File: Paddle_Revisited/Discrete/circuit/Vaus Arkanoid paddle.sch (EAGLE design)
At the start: 22 parts, among them IC1 4040N, IC2 74165N, IC3 74LS00N, IC4 LM556N

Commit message: Cleanup and organization of some directories
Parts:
- added C9: 100nf, rcl:C-EU050-024X044
- C2: value 15n -> 10n
- R3: value 1k -> 1k5
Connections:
- net DOUT: now also C9.1
- net GND: now also C9.2
- net N$15: now also R5.A; no longer R5.E
- net N$22: now also R5.E; no longer R5.A
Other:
- note added: "VAUS ARKANOID PADDLE FOR MSX"
- note removed: "TAITO ARKANOID PADDLE FOR MSX"
- moved on the sheet: K1

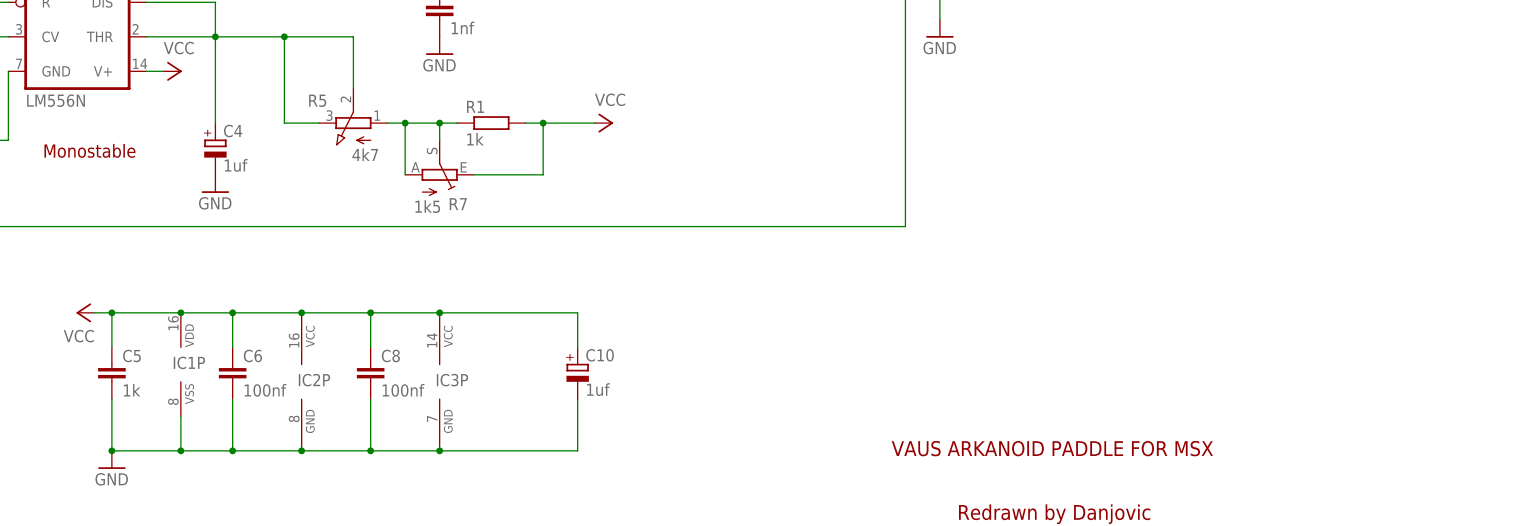
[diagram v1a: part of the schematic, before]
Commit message: Updated component values
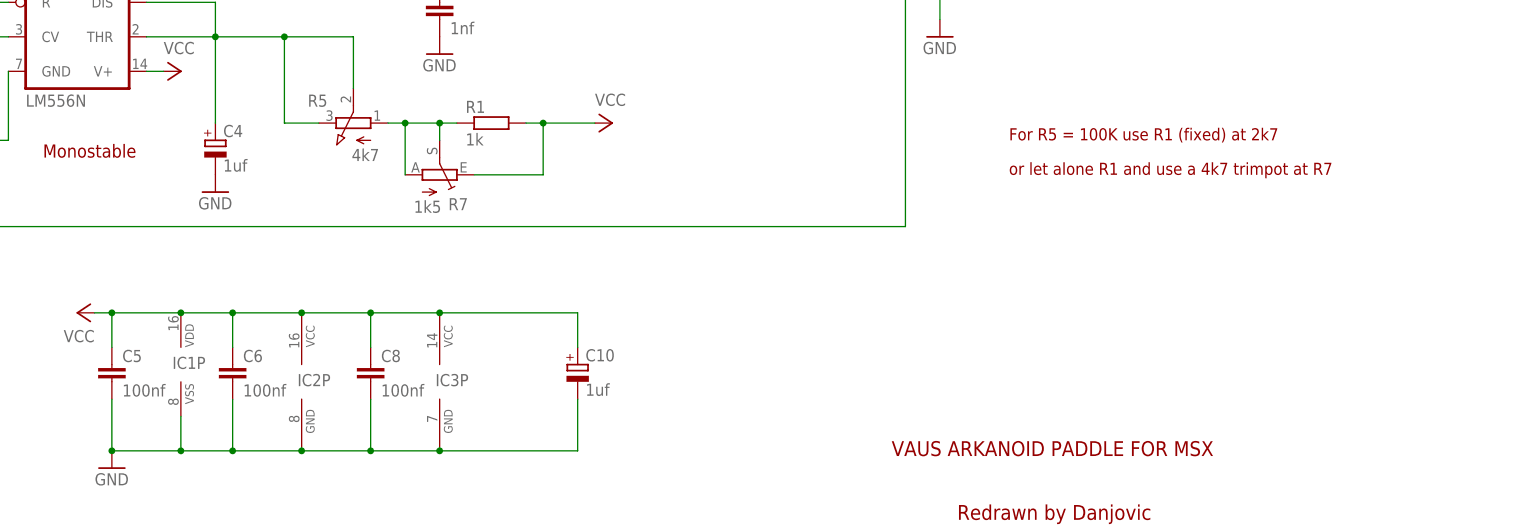
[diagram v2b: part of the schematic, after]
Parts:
- C5: value 1k -> 100nf
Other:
- note added: "For R5 = 100K use R1 (fixed) at 2k7"
- note added: "or let alone R1 and use a 4k7 trimpot at R7"
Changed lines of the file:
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@@
 <part name="P+8" library="supply1" deviceset="VCC" device=""/>
 <part name="C4" library="rcl" deviceset="CPOL-EU" device="E2-4" value="1uf"/>
-<part name="C5" library="rcl" deviceset="C-EU" device="050-024X044" value="1k"/>
+<part name="C5" library="rcl" deviceset="C-EU" device="050-024X044" value="100nf"/>
 <part name="C6" library="rcl" deviceset="C-EU" device="050-024X044" value="100nf"/>
 <part name="C8" library="rcl" deviceset="C-EU" device="050-024X044" value="100nf"/>
@@
 <text x="163.068" y="19.558" size="2.1844" layer="94">VAUS ARKANOID PADDLE FOR MSX</text>
 <text x="172.72" y="10.16" size="2.1844" layer="94">Redrawn by Danjovic</text>
+<text x="180.34" y="66.04" size="1.778" layer="94" font="vector">For R5 = 100K use R1 (fixed) at 2k7</text>
+<text x="180.34" y="60.96" size="1.778" layer="94" font="vector">or let alone R1 and use a 4k7 trimpot at R7</text>
 </plain>
 <instances>
